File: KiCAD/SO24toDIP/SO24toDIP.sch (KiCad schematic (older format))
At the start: 2 parts, among them U1 STP8DP05, U2 STP16DP05

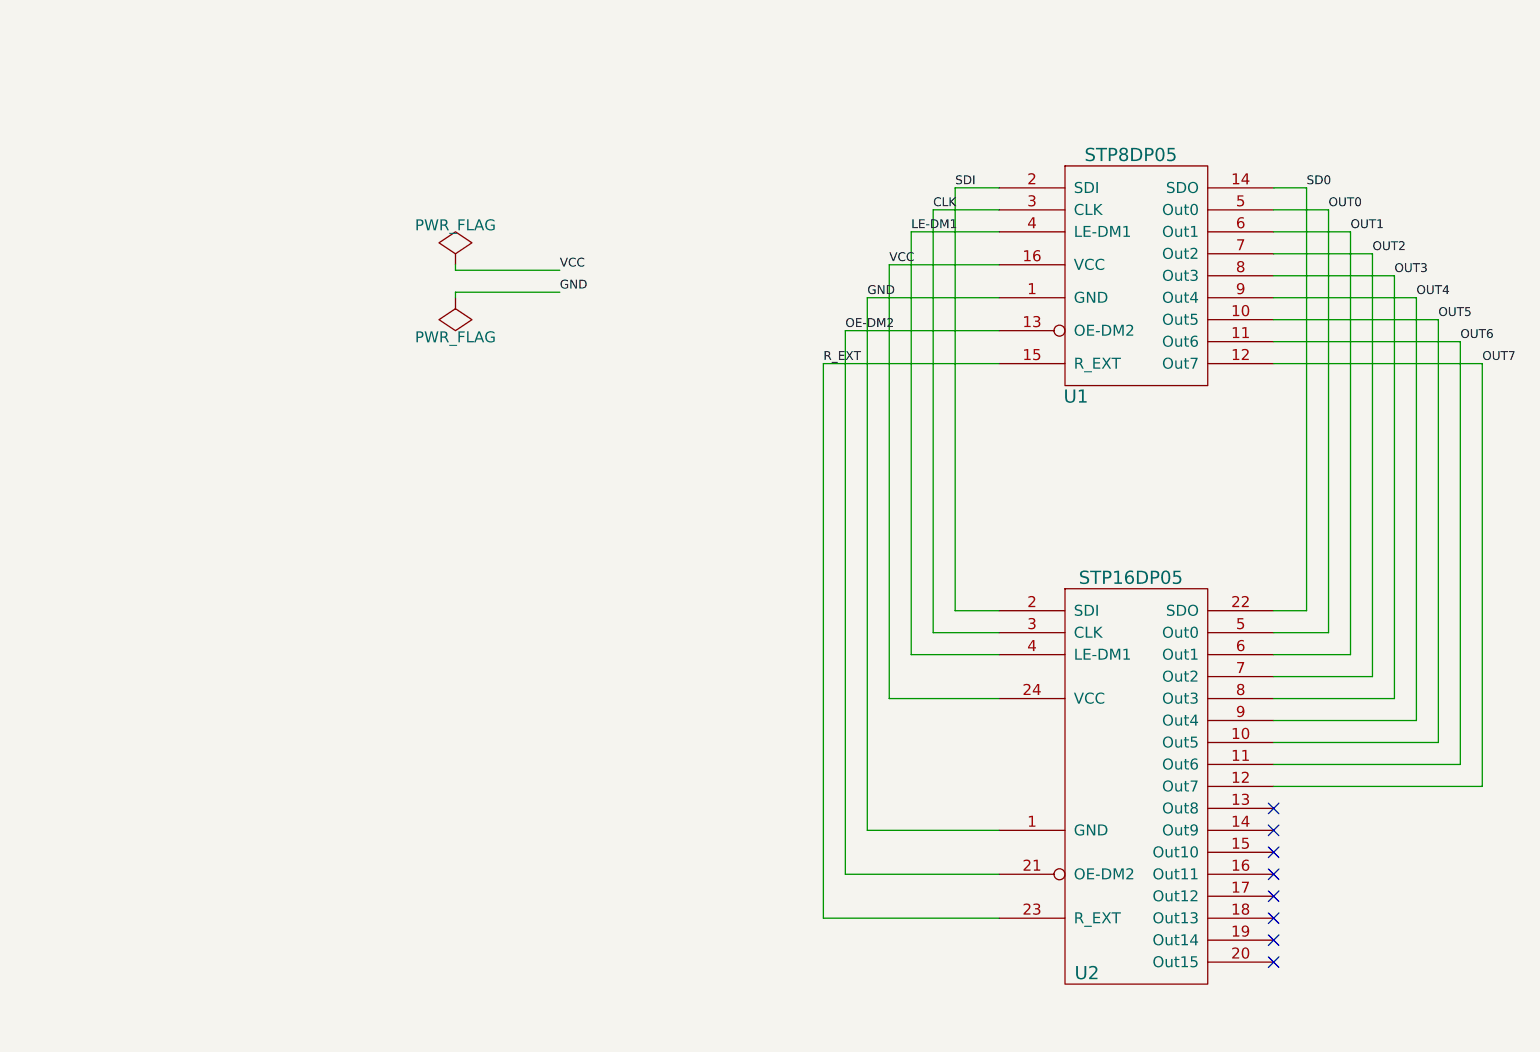
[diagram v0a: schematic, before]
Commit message: added 24-SOIC to 24-DIP breakout board for 74HC154
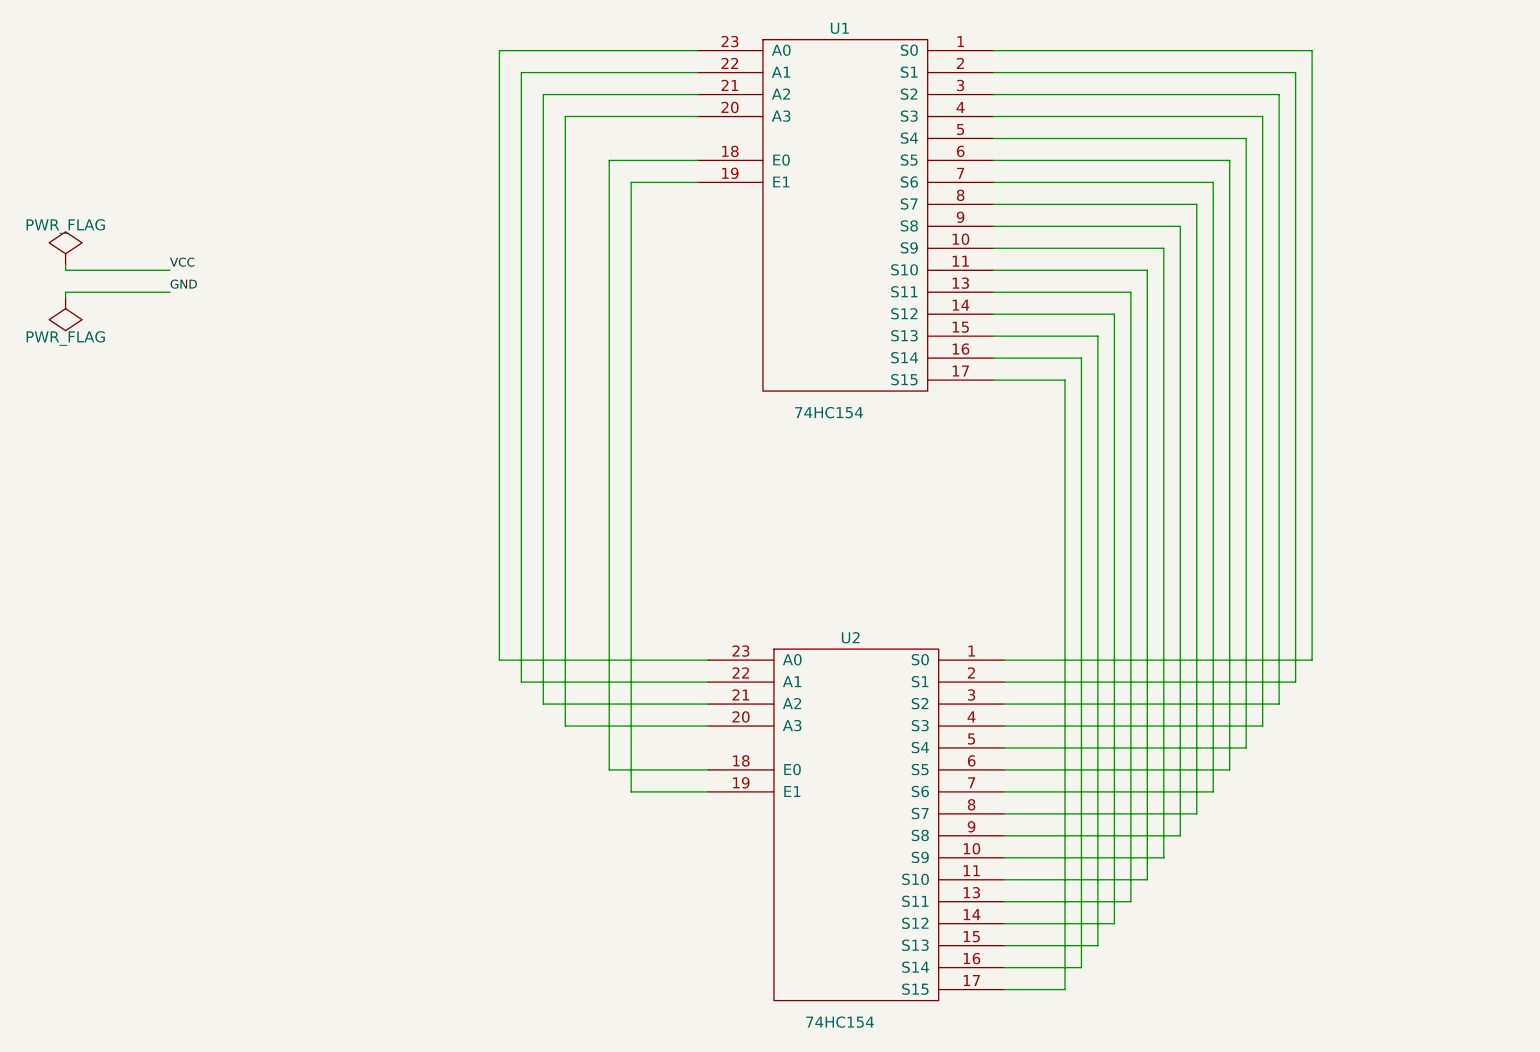
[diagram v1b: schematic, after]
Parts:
- removed U1: STP8DP05, soic2dip_libs:SOIC-16_3.9x9.9mm_Pitch1.27mm, symbol STP8DP05
- removed U2: STP16DP05, soic2dip_libs:DIP-24_600_ELL, symbol STP16DP05
- added U1: 74HC154, SO24toDIP_libs:DIP-24_W15.24mm_LongPads, symbol 74LS154
- added U2: 74HC154, SO24toDIP_libs:SOIC-24_7.5x15.4mm_Pitch1.27mm, symbol 74LS154
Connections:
- net GND: now also U1.12 (GND), U2.12 (GND)
- net VCC: now also U1.24 (VCC), U2.24 (VCC)
- new net: U1.1 (S0), U2.1 (S0)
- new net: U1.10 (S9), U2.10 (S9)
- new net: U1.11 (S10), U2.11 (S10)
- new net: U1.13 (S11), U2.13 (S11)
- new net: U1.14 (S12), U2.14 (S12)
- new net: U1.15 (S13), U2.15 (S13)
- new net: U1.16 (S14), U2.16 (S14)
- new net: U1.17 (S15), U2.17 (S15)
- new net: U1.18 (E0), U2.18 (E0)
- new net: U1.19 (E1), U2.19 (E1)
- new net: U1.2 (S1), U2.2 (S1)
- new net: U1.20 (A3), U2.20 (A3)
- new net: U1.21 (A2), U2.21 (A2)
- new net: U1.22 (A1), U2.22 (A1)
- new net: U1.23 (A0), U2.23 (A0)
- new net: U1.3 (S2), U2.3 (S2)
- new net: U1.4 (S3), U2.4 (S3)
- new net: U1.5 (S4), U2.5 (S4)
- new net: U1.6 (S5), U2.6 (S5)
- new net: U1.7 (S6), U2.7 (S6)
- new net: U1.8 (S7), U2.8 (S7)
- new net: U1.9 (S8), U2.9 (S8)
- no-connect marks 8 -> 0
